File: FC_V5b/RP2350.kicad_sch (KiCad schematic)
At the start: 27 parts, among them U11 W25Q128JVS, U18 RP2350_60QFN, Y1 ABM8-272-T3

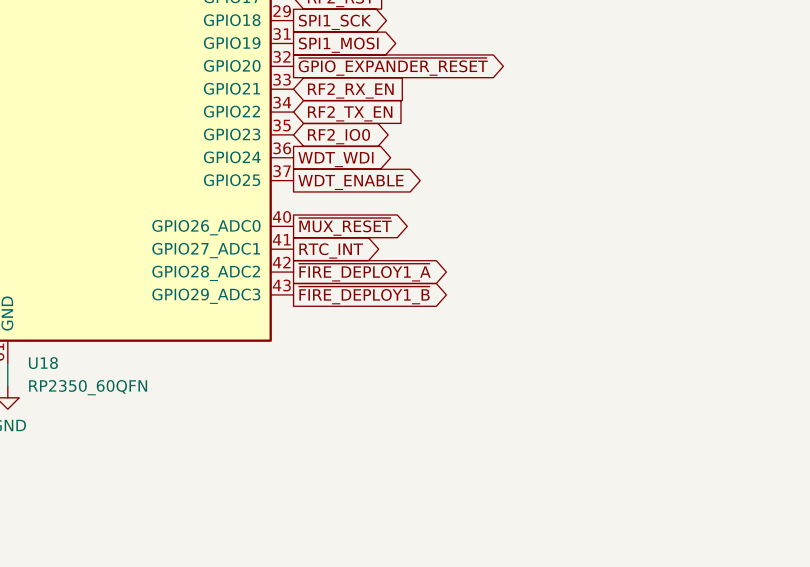
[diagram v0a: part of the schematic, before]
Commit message: Added TPS2 and TPS4 Load Switch Schematics
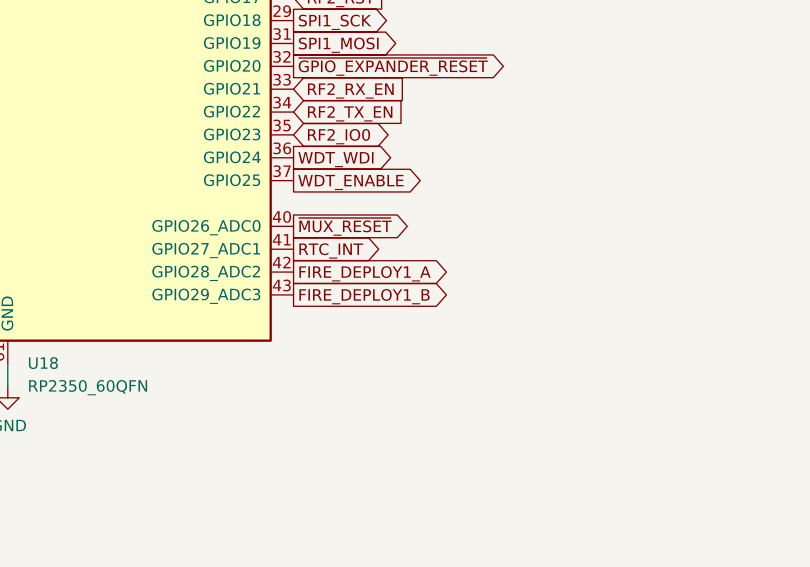
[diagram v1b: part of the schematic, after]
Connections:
- net ~{FIRE_DEPLOY1_A} renamed FIRE_DEPLOY1_A
- net ~{FIRE_DEPLOY1_B} renamed FIRE_DEPLOY1_B
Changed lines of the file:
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@@
 		)
 	)
-	(global_label "~{FIRE_DEPLOY1_A}"
+	(global_label "FIRE_DEPLOY1_A"
 		(shape output)
 		(at 209.55 146.05 0)
@@
 		)
 	)
-	(global_label "~{FIRE_DEPLOY1_B}"
+	(global_label "FIRE_DEPLOY1_B"
 		(shape output)
 		(at 209.55 148.59 0)
